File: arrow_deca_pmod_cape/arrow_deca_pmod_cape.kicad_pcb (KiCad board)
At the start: 4 copper layers, 73.7 x 62 mm, 12 parts, among them J1 PMOD_A, J10 Conn_02x01, J11 Conn_02x01, J12 Conn_02x01, J2 P8_Male, J3 P9_Male, J4 PMOD_B, J5 PMOD_C, J6 PMOD_D, J7 PMOD_E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

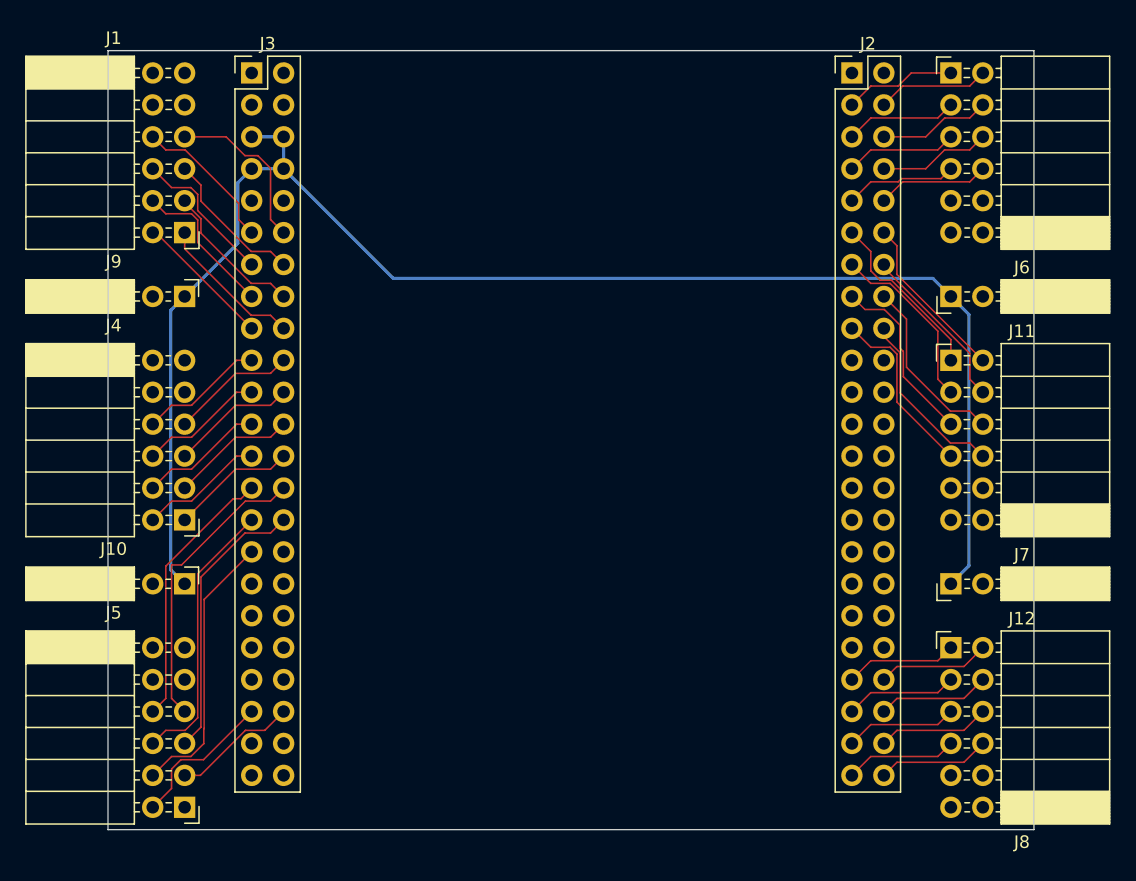
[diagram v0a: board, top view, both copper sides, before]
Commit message: Move labels.
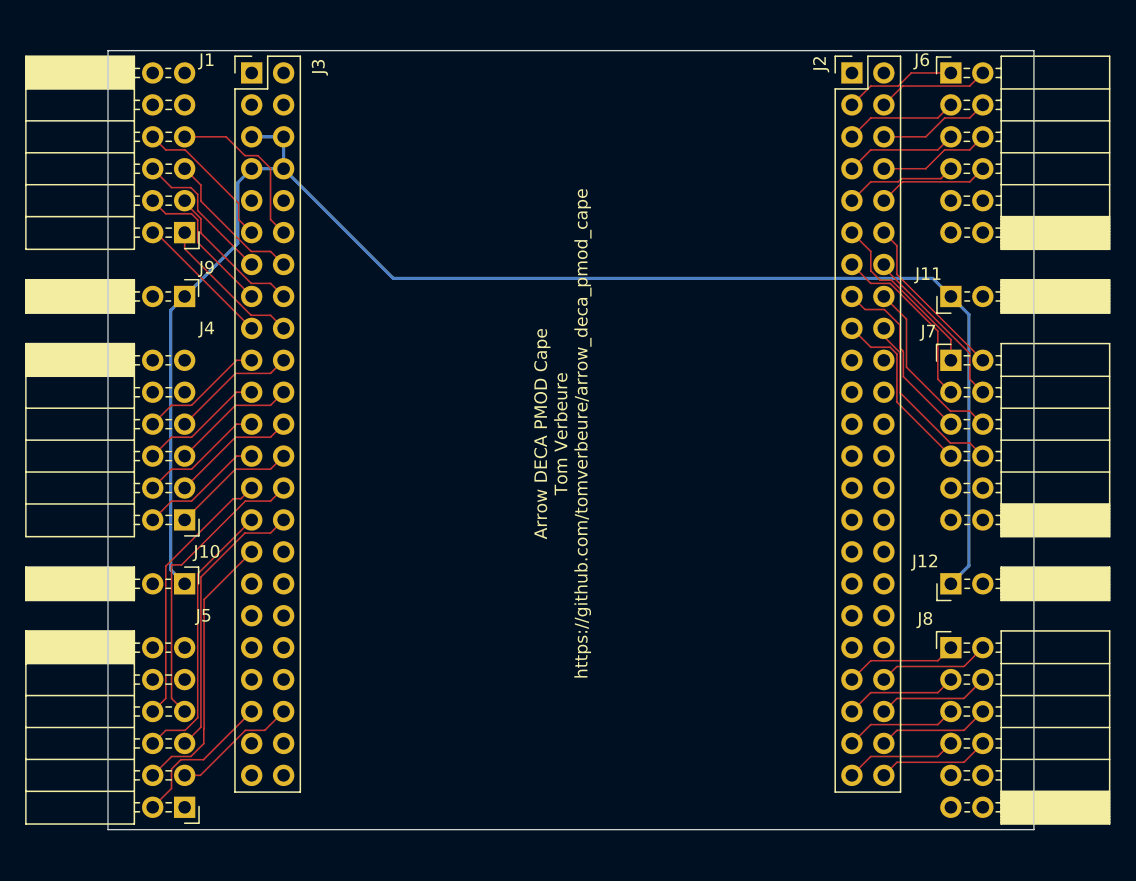
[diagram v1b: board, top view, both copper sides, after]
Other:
- board text added: "Arrow DECA PMOD Cape Tom Verbeure https://github.com/tomverbeure/arrow_deca_pmod_cape"
